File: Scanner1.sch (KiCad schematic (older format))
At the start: 45 parts, among them J1 USB_B_Mini, J2 Conn_02x05_Odd_Even, J3 Conn_02x03_Odd_Even, Q1 MOSFET_N, SW1 SW_PUSHBUTTON, SW2 SW_DPST, SW3 SW_DPST, U1 ATmega32U4-AU, Y1 16 MHz X322516MLB4SI

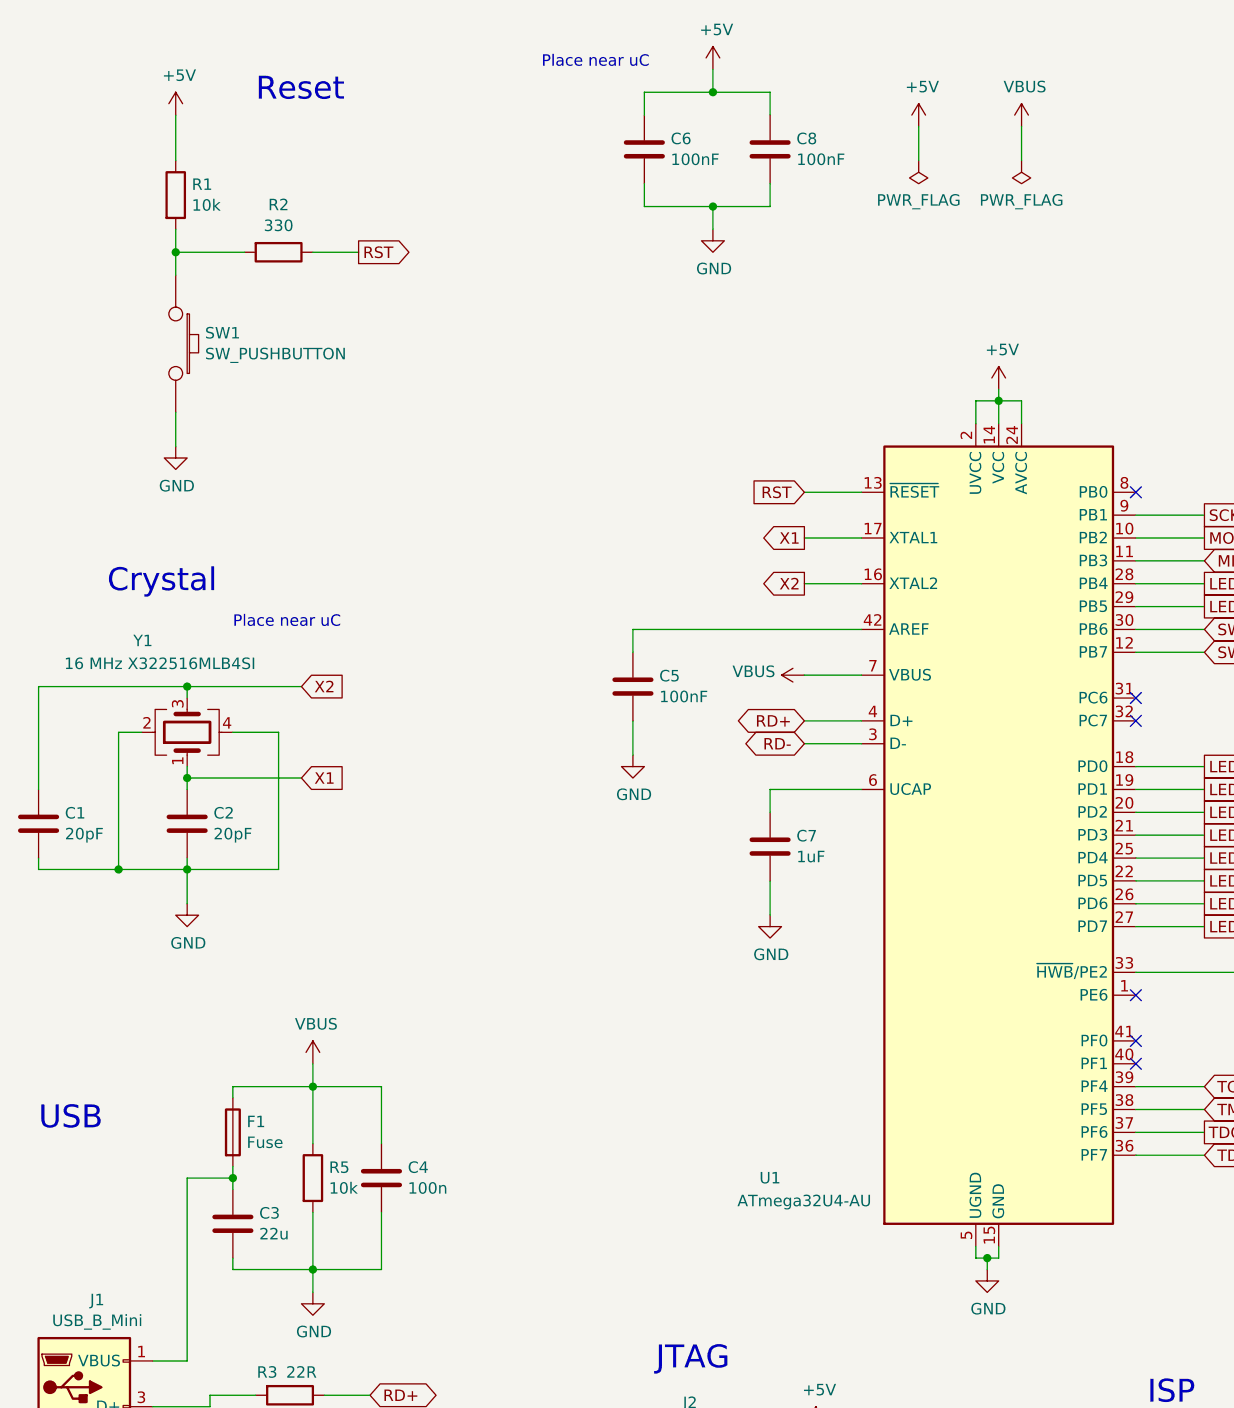
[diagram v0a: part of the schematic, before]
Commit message: Assign all footprints and JLCPCB part numbers. Generate BOM and netlist (netlist not included in repo)
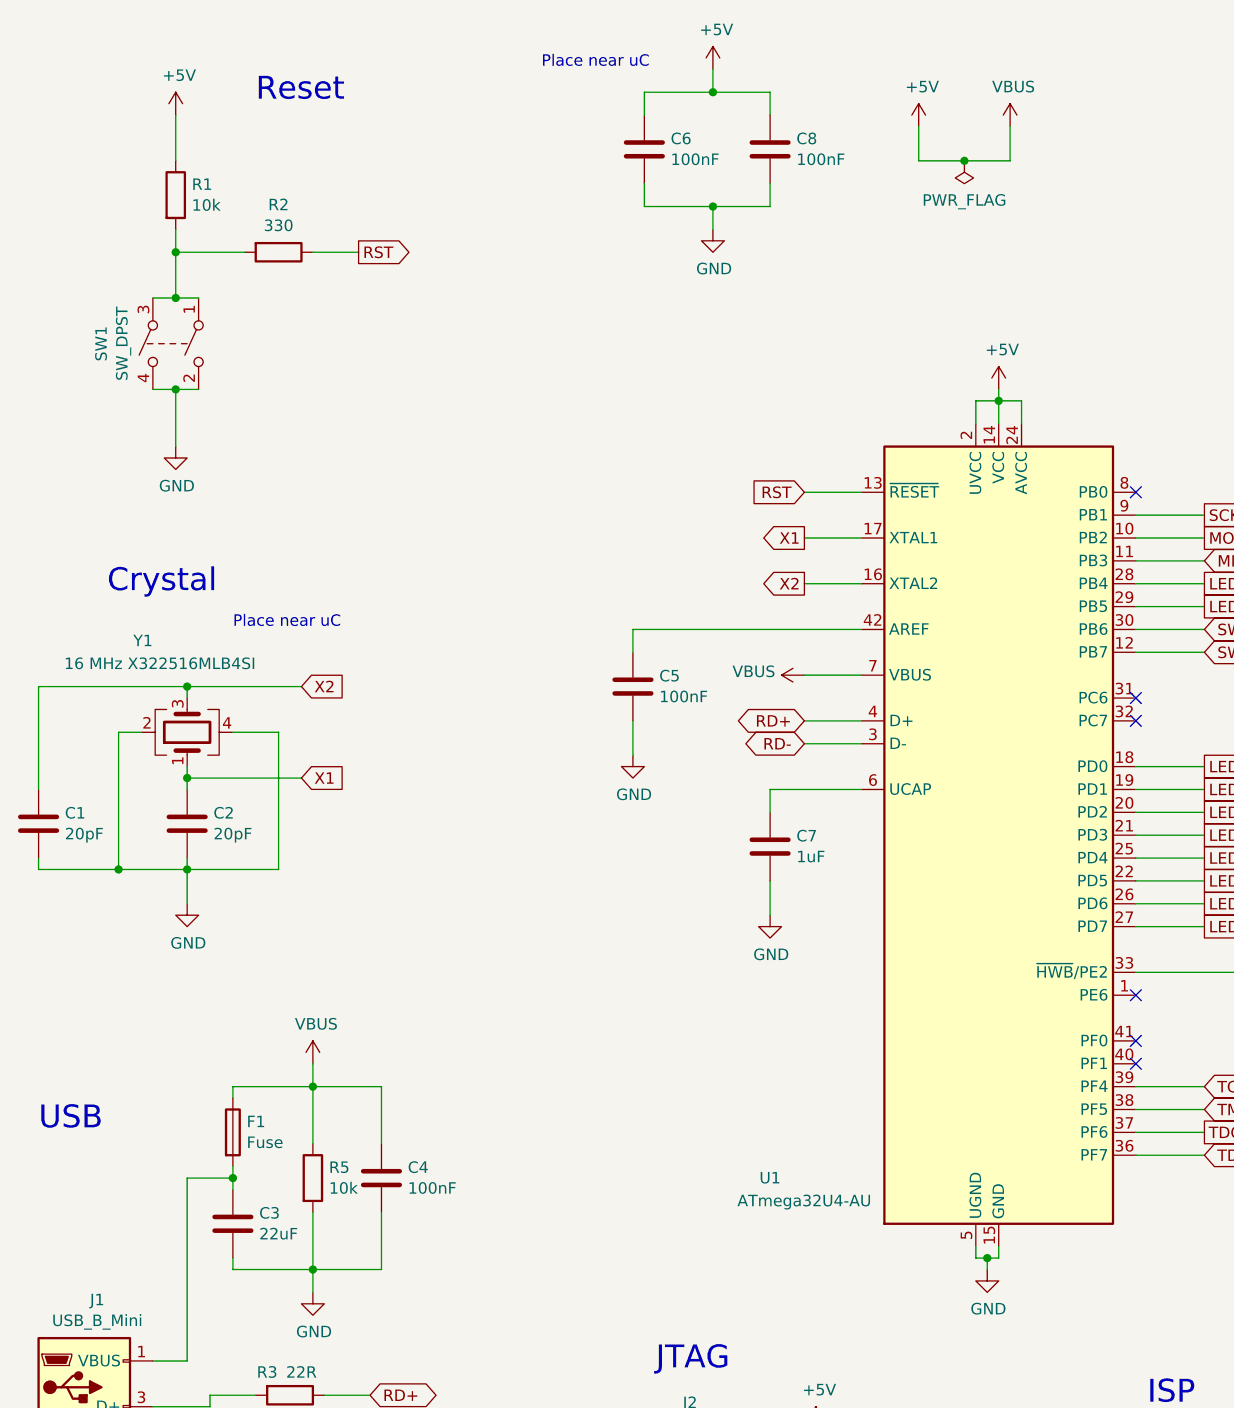
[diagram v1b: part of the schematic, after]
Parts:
- removed SW1: SW_PUSHBUTTON, symbol freetronics_schematic:SW_PUSHBUTTON
- added SW1: SW_DPST, Button_Switch_THT:SW_PUSH_6mm_H7.3mm, symbol Switch:SW_DPST
- C1, C2: footprint (none) -> Capacitor_SMD:C_0805_2012Metric; LCSC Part # (none) -> C1798
- C3: value 22u -> 22uF; footprint (none) -> Capacitor_SMD:C_0805_2012Metric; LCSC Part # (none) -> C45783
- C4: value 100n -> 100nF; footprint (none) -> Capacitor_SMD:C_0805_2012Metric; LCSC Part # (none) -> C49678
- C5, C6, C8: footprint (none) -> Capacitor_SMD:C_0805_2012Metric; LCSC Part # (none) -> C49678
- C7: footprint (none) -> Capacitor_SMD:C_0805_2012Metric; LCSC Part # (none) -> C28323
- D1, D2, D3, D4, D5, D6, D7, D8, D9: footprint (none) -> LED_SMD:LED_0805_2012Metric; LCSC Part # (none) -> C2293
- F1: footprint (none) -> Fuse:Fuse_0805_2012Metric; LCSC Part # (none) -> C116170
- J1: footprint (none) -> digikey-footprints:USB_Mini_B_Female_548190519; DigiKey Part # (none) -> 0548190519
- J2: footprint (none) -> Connector_PinHeader_2.54mm:PinHeader_2x03_P2.54mm_Vertical
- J3: footprint (none) -> Connector_PinHeader_2.54mm:PinHeader_2x05_P2.54mm_Vertical
- Q1: footprint (none) -> Package_TO_SOT_SMD:SOT-23; LCSC Part # (none) -> C20917
- R1, R18, R5, R6, R7, R8: footprint (none) -> Resistor_SMD:R_0805_2012Metric; LCSC Part # (none) -> C17414
- R10, R11, R12, R13, R14, R15, R16, R17, R2, R9: footprint (none) -> Resistor_SMD:R_0805_2012Metric; LCSC Part # (none) -> C17630
- R3, R4: footprint (none) -> Resistor_SMD:R_0805_2012Metric; LCSC Part # (none) -> C17561
- SW2, SW3: footprint (none) -> Button_Switch_THT:SW_PUSH_6mm_H7.3mm
- U1: LCSC Part # (none) -> C44854
- Y1: footprint (none) -> Crystal:Crystal_SMD_3225-4Pin_3.2x2.5mm; LCSC Part # (none) -> C13738
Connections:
- net VBUS is gone; now on net +5V: C4.1, F1.1, R5.1, U1.7 (VBUS)
- net GND: now also SW1.2, SW1.4
- net at R1.2, R2.2: now also SW1.1, SW1.3

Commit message: Fix issues with footprints vs symbols (some didn't line up, had to change some footprints and some symbols) and start layout
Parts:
- removed J1: USB_B_Mini, digikey-footprints:USB_Mini_B_Female_548190519, symbol Connector:USB_B_Mini
- added J1: 0548190519, digikey-footprints:USB_Mini_B_Female_548190519, symbol dk_USB-DVI-HDMI-Connectors:0548190519
- J2: footprint Connector_PinHeader_2.54mm:PinHeader_2x03_P2.54mm_Vertical -> Connector_PinHeader_2.54mm:PinHeader_2x05_P2.54mm_Vertical
- J3: footprint Connector_PinHeader_2.54mm:PinHeader_2x05_P2.54mm_Vertical -> Connector_PinHeader_2.54mm:PinHeader_2x03_P2.54mm_Vertical
- Q1: symbol freetronics_schematic:MOSFET_N -> Device:Q_NMOS_GSD
- SW1, SW2, SW3: value SW_DPST -> SW_Push; symbol Switch:SW_DPST -> Switch:SW_Push
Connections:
- net +5V: no longer SW2.4, SW3.4
- net GND: now also Q1.2 (S), J1.5, J1.SH; no longer Q1.S, SW1.4
- net LED_CTRL: now also Q1.1 (G); no longer Q1.G
- net RD+: now also R4.1; no longer R3.1
- net RD-: now also R3.1; no longer R4.1
- net SW_0: no longer SW2.3
- net SW_1: no longer SW3.3
- net at R1.2, R2.2, SW1.1: no longer SW1.3
- net at D1.1 (K), D2.1 (K), D3.1 (K)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: now also Q1.3 (D); no longer Q1.D
- net VBUS: now reaches C3.1, F1.2
- net VBUS: now also J1.1
- net at R4.2: now also J1.3
- net at R3.2: now also J1.2

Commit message: More layout
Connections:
- net SW_0: now also U1.8 (PB0); no longer U1.30 (PB6)
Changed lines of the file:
@@
 Wire Wire Line
 	9100 4950 9350 4950
-Text GLabel 6050 3250 2    50   Input ~ 0
+Text GLabel 6050 2650 2    50   Input ~ 0
 SW_0
 Text GLabel 6050 3350 2    50   Input ~ 0
 SW_1
-Wire Wire Line
-	6050 3250 5750 3250
 Wire Wire Line
 	5750 3350 6050 3350
@@
 Wire Wire Line
 	9800 5850 9800 6000
-NoConn ~ 5750 2650
+NoConn ~ 5750 3250
 NoConn ~ 5750 3550
 NoConn ~ 5750 3650
@@
 Text Label 1550 6150 1    50   ~ 0
 VBUS
+Wire Wire Line
+	6050 2650 5750 2650
 $EndSCHEMATC
